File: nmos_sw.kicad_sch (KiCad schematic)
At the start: 6 parts, among them Q3 BUZ11

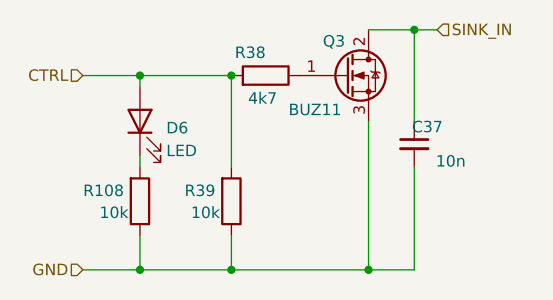
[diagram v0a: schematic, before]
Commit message: routing mostly done, fixing schematic issues
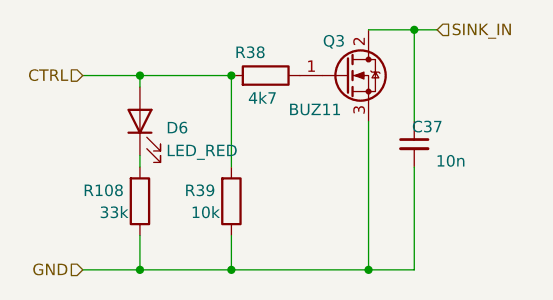
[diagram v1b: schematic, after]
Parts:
- D6: value LED -> LED_RED; footprint Diode_SMD:D_0603_1608Metric -> LED_SMD:LED_0603_1608Metric
- R108: value 10k -> 33k
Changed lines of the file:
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@@
       (effects (font (size 1.27 1.27)) (justify right))
     )
-    (property "Value" "10k" (id 1) (at 55.88 69.85 0)
+    (property "Value" "33k" (id 1) (at 55.88 69.85 0)
       (effects (font (size 1.27 1.27)) (justify right))
     )
@@
       (effects (font (size 1.27 1.27)) (justify right))
     )
-    (property "Value" "LED" (id 1) (at 60.071 62.9797 90)
+    (property "Value" "LED_RED" (id 1) (at 60.071 62.9797 90)
       (effects (font (size 1.27 1.27)) (justify right))
     )
-    (property "Footprint" "Diode_SMD:D_0603_1608Metric" (id 2) (at 57.15 59.69 0)
+    (property "Footprint" "LED_SMD:LED_0603_1608Metric" (id 2) (at 57.15 59.69 0)
       (effects (font (size 1.27 1.27)) hide)
     )
